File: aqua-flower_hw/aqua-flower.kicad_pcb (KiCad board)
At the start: 2 copper layers, 44 parts, among them Q1 NPN, Q2 IRLML6302, Q3 IRLML6302, Q4 IRLML6302, Q5 IRLML6302, SW1 BUTTON, SW2 BUTTON, SW3 BUTTON, SW4 BUTTON, SW5 BUTTON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

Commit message: Now everything is ok. + Add library by the library Wizard. + Found needed in KiCad github.
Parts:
- C1, C10, C11, C2, C3, C4, C5, C6, C7, C8, C9: footprint Capacitors_SMD:C_0603_HandSoldering -> Capacitors:CAP_0603
- DD1: footprint Housings_QFP:LQFP-48_7x7mm_Pitch0.5mm -> LQFP_TQFP:LQFP48
- R1, R2, R3, R4, R5: footprint Resistors_SMD:R_0603_HandSoldering -> Resistors:RES_0603
- moved HOLE1 68.3 mm to (215.9, 110.5)
- moved C6 61.4 mm to (156.0, 104.5)
- moved C7 61.0 mm to (152.4, 104.5)
- moved DD1 58.6 mm to (188.9, 63.5)
- moved SW6 56.4 mm to (207.3, 62.5)
- moved SW2 55.4 mm to (182.5, 98.5)
- moved C9 54.0 mm to (148.9, 104.5)
- moved C4 53.2 mm to (159.5, 106.0)
- moved HOLE2 51.9 mm to (120.7, 58.4)
- moved HOLE3 49.2 mm to (120.7, 108.0)
- moved C2 48.5 mm to (166.6, 106.0)
- moved R2 43.6 mm to (189.0, 95.5)
- moved C1 40.6 mm to (170.2, 104.7)
- moved XL5 38.6 mm to (136.0, 101.3)
- moved C3 38.3 mm to (163.1, 106.0)
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
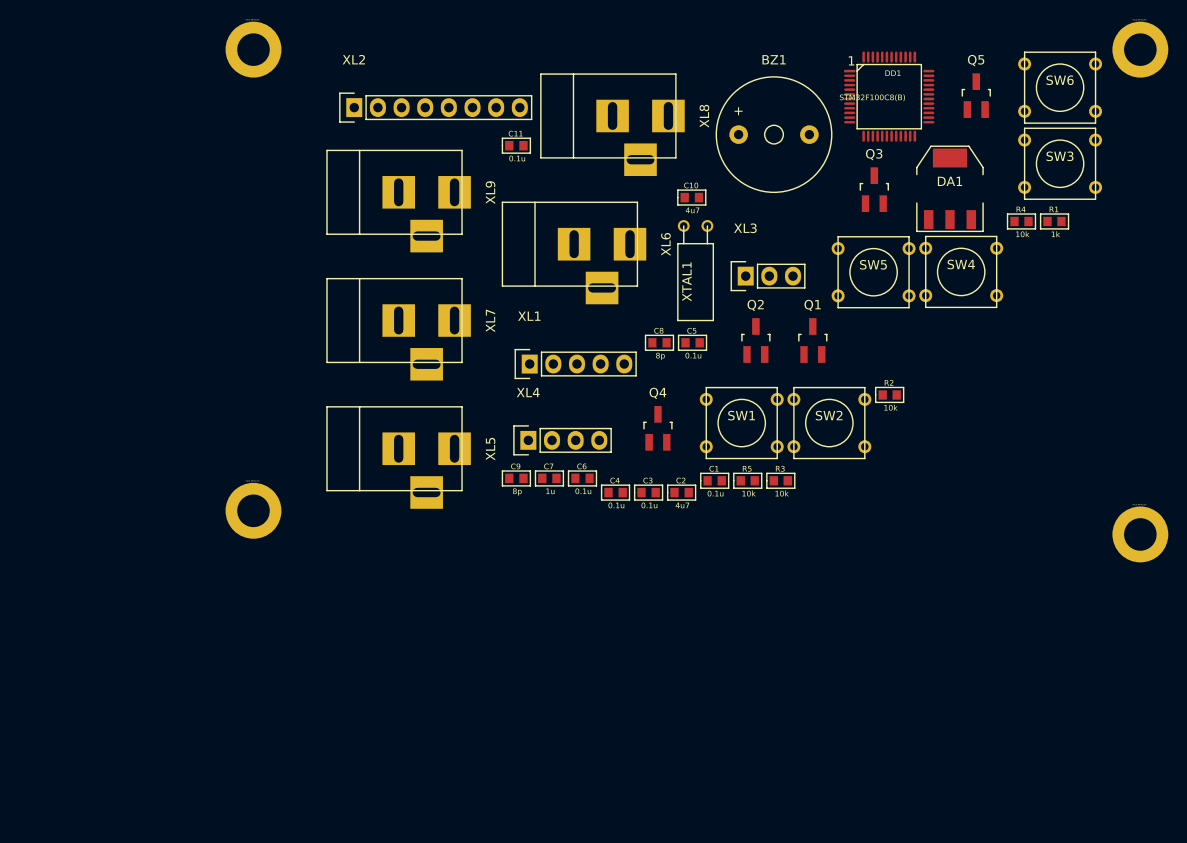
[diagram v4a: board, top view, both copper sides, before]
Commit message: Export to TopoR from KiCAD
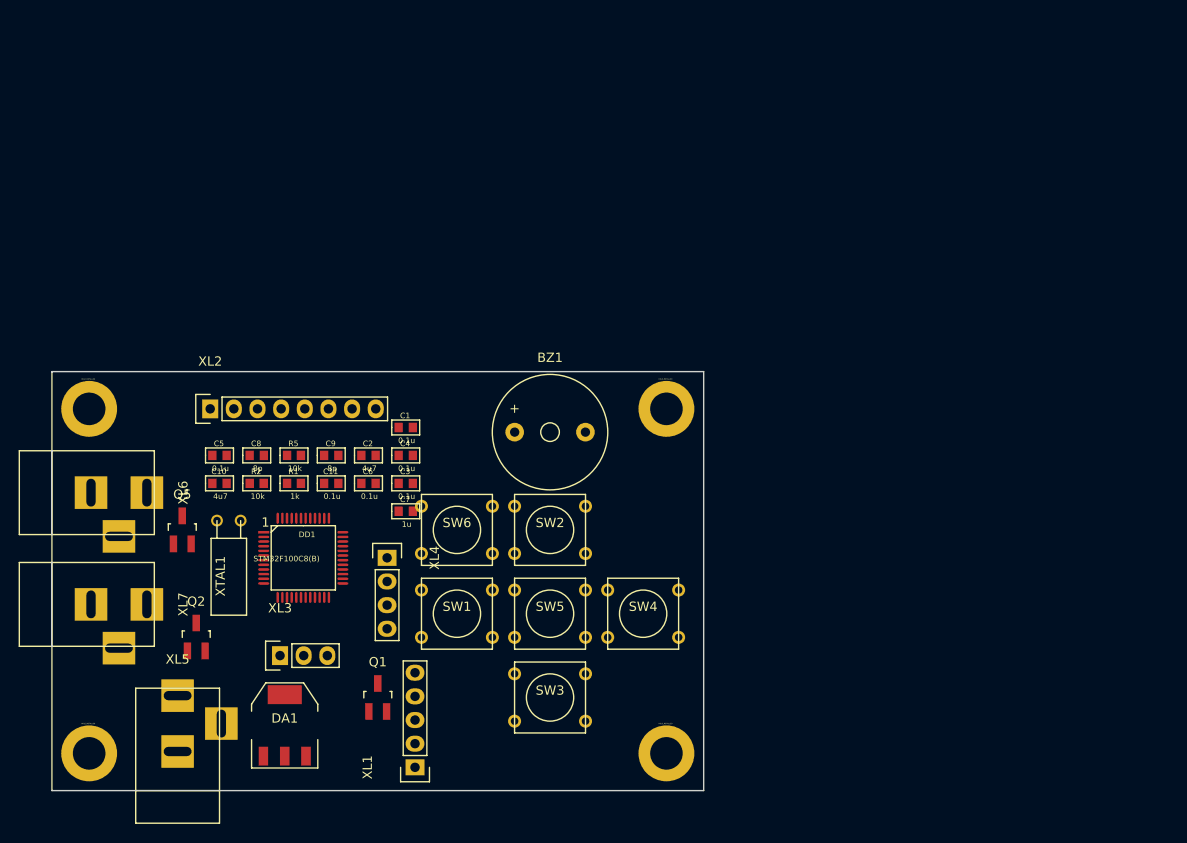
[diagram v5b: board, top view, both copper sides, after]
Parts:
- removed Q3, Q4: IRLML6302, TO_SOT_Packages_SMD:SOT-23_Handsoldering
- removed R3, R4: 10k, Resistors:RES_0603
- removed XL8, XL9: CONN_3, Connect:BARREL_JACK
- moved HOLE4 119.3 mm to (103.0, 97.0)
- moved Q5 97.2 mm to (113.0, 110.0)
- moved DA1 91.8 mm to (124.0, 131.0)
- moved R1 86.4 mm to (125.0, 105.0)
- moved SW6 80.3 mm to (142.5, 110.0)
- moved DD1 80.1 mm to (126.0, 113.0)
- moved SW3 79.3 mm to (152.5, 128.0)
- moved R2 68.6 mm to (121.0, 105.0)
- moved Q2 68.0 mm to (114.5, 121.5)
- moved XL3 64.5 mm to (123.5, 123.5)
- moved Q1 60.4 mm to (134.0, 128.0)
- moved C10 59.3 mm to (117.0, 105.0)
- moved XTAL1 59.3 mm to (118.0, 109.0)
- moved HOLE2 58.8 mm to (165.0, 97.0)
- moved XL6 58.3 mm to (103.0, 106.0)
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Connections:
- DD1 pad 12: /CH3_POWER -> Net-(DD1-Pad12)
- DD1 pad 13: /CH4_POWER -> Net-(DD1-Pad13)
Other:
- board outline added: 70 x 45 mm

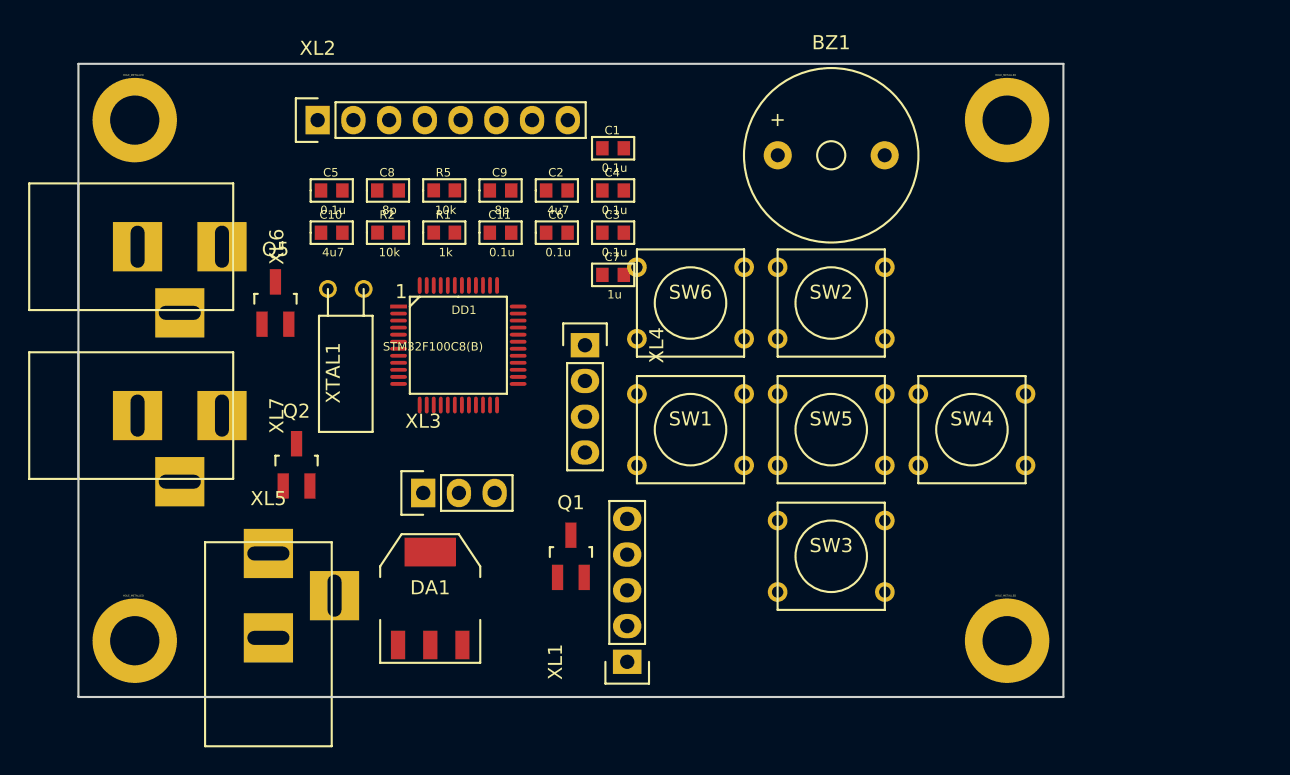
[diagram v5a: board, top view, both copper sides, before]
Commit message: Add eeprom
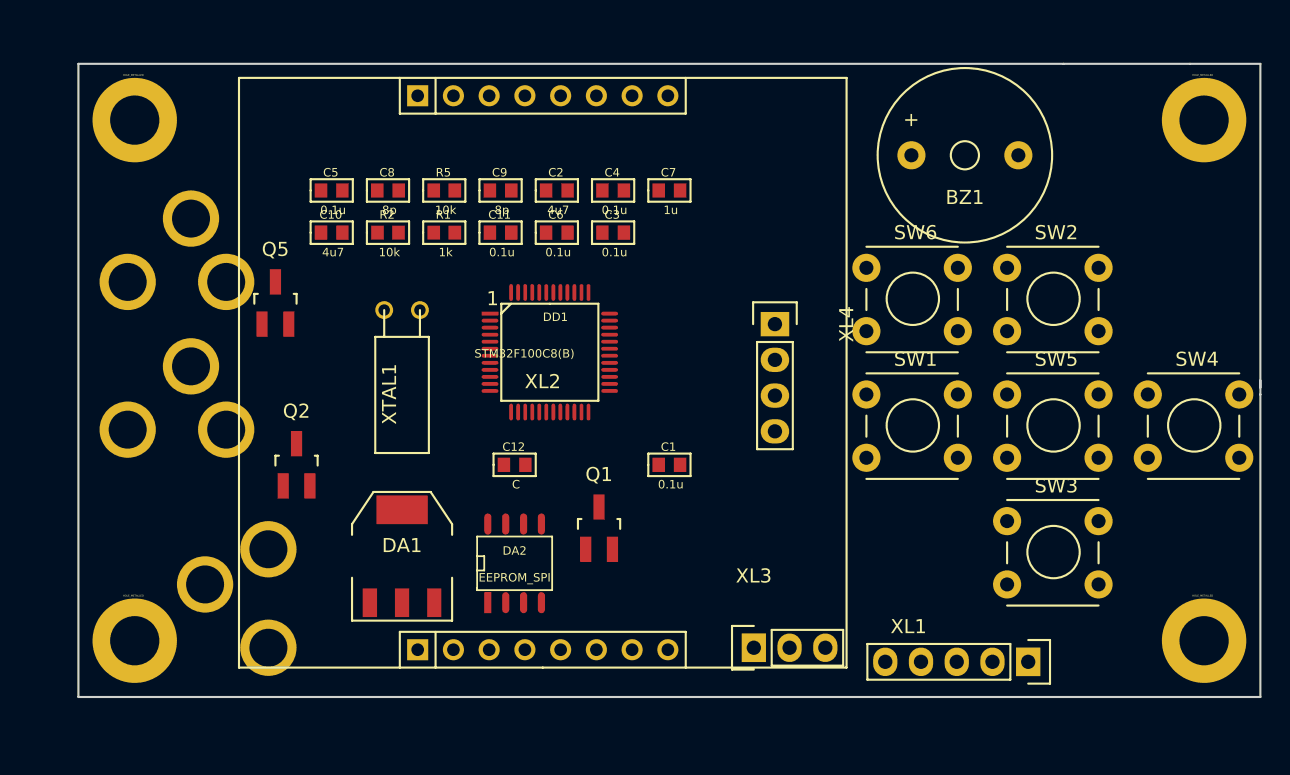
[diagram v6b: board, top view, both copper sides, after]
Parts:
- added C12: C, Capacitors:CAP_0603, F.Cu at (130.0, 121.5)
- added DA2: EEPROM_SPI, SO_DIL_TSSOP:SO8, F.Cu at (130.0, 128.5)
- SW1, SW2, SW3, SW4, SW5, SW6: footprint Buttons_Switches_ThroughHole:SW_PUSH_SMALL -> BtnsSwitches:PUSH_THRHOLE_3-1825910-5
- XL2: footprint Socket_Strips:Socket_Strip_Straight_1x08 -> Display:84x48_LCD_Module
- XL5, XL6, XL7: value CONN_3 -> BARREL_SOCKET; footprint Connect:BARREL_JACK -> Connectors:Barrel; moved to B.Cu
- moved XL1 28.5 mm to (166.5, 135.5), turned to 180 degrees
- moved XL3 25.9 mm to (147.0, 134.5)
- moved XL5 25.7 mm to (109.5, 108.5), turned to 0 degrees
- moved C1 22.9 mm to (141.0, 121.5)
- moved XL2 16.3 mm to (132.0, 94.0)
- moved XL6 14.5 mm to (109.5, 119.0)
- moved HOLE1 14.0 mm to (179.0, 134.0)
- moved HOLE2 14.0 mm to (179.0, 97.0)
- moved XL4 13.6 mm to (148.5, 111.5)
- moved XL7 13.4 mm to (112.5, 127.5), turned to 90 degrees
- moved SW1 12.3 mm to (154.5, 121.5)
- moved SW2 12.3 mm to (164.5, 112.5)
- moved SW3 12.3 mm to (164.5, 130.5)
- moved SW4 12.3 mm to (174.5, 121.5)
- moved SW5 12.3 mm to (164.5, 121.5)
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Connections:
- DD1 pad 12: Net-(DD1-Pad12) -> /EE_HOLD
- DD1 pad 13: Net-(DD1-Pad13) -> /EE_WP
- DD1 pad 42: Net-(DD1-Pad42) -> /EE_CS
- DD1 pad 43: Net-(DD1-Pad43) -> /EE_MISO
- DD1 pad 45: Net-(DD1-Pad45) -> /EE_MOSI
- DD1 pad 46: Net-(DD1-Pad46) -> /EE_SCK
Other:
- board size 70 x 45 mm -> 84 x 45 mm

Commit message: Replace straight pin connectors
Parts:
- XL1: footprint Socket_Strips:Socket_Strip_Straight_1x05 -> Connectors:PLS-5
- XL3: footprint Socket_Strips:Socket_Strip_Straight_1x03 -> Connectors:PLS-3
- XL4: footprint Socket_Strips:Socket_Strip_Straight_1x04 -> Connectors:PLS-4
- moved XL7 20.7 mm to (109.5, 107.0), turned to 0 degrees
- moved XL5 19.3 mm to (113.0, 127.5), turned to 90 degrees
- moved C3 16.3 mm to (135.5, 121.2), turned to 180 degrees
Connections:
- Q2 pad 3: Net-(Q2-Pad3) -> /12V
- Q5 pad 3: Net-(Q5-Pad3) -> /12V
- XL6 pad PWR: Net-(Q5-Pad3) -> /12V
- XL7 pad PWR: Net-(Q2-Pad3) -> /12V
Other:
- outline, holes or cut-outs redrawn
- net class 12V added: clearance 0.3, trace_width 0.7, via_dia 0.8, via_drill 0.4
- net class Default: via_dia 0.6 -> 0.8
- net class PWR added: clearance 0.3, trace_width 0.5, via_dia 0.8, via_drill 0.4
- rule via_min_size: 0.4 -> 0.7

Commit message: PCB finalize. Ready to production.
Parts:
- C10: value 4u7 -> 10u; footprint Capacitors:CAP_0603 -> Capacitors:CAP_0805
- C12: value C -> 0.1u
- XL1: value CONN_5 -> CONN_6; footprint Connectors:PLS-5 -> Connectors:PLS-6
- moved XL1 49.5 mm to (121.4, 115.0), turned to 90 degrees
- moved XL3 35.1 mm to (155.3, 100.4), turned to 90 degrees
- moved Q1 27.3 mm to (152.1, 104.0), turned to 270 degrees
- moved C5 25.9 mm to (142.2, 108.1), turned to 270 degrees
- moved DA2 22.7 mm to (147.9, 114.6)
- moved C12 20.4 mm to (145.4, 108.1), turned to 270 degrees
- moved C10 19.5 mm to (116.8, 124.5), turned to 270 degrees
- moved C4 19.3 mm to (137.0, 121.3)
- moved C2 19.2 mm to (126.7, 120.1), turned to 270 degrees
- moved R5 16.9 mm to (116.0, 116.3), turned to 180 degrees
- moved XL4 16.9 mm to (155.2, 127.0)
- moved R1 15.9 mm to (140.6, 108.1), turned to 270 degrees
- moved C11 15.6 mm to (125.1, 120.1), turned to 270 degrees
- moved XTAL1 14.6 mm to (134.6, 103.2), turned to 90 degrees
- moved Q2 14.5 mm to (115.2, 107.0), turned to 90 degrees
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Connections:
- Q2 pad 3: /12V -> /PUMP2
- Q5 pad 3: /12V -> /PUMP1
- XL1 pad 2: /CC_SCK -> /CC_MOSI
- XL1 pad 3: /CC_CS -> /CC_MISO
- XL1 pad 4: /CC_MISO -> /CC_SCK
- XL1 pad 5: /CC_MOSI -> /CC_CS
- XL6 pad PWR: /12V -> /PUMP1
- XL7 pad PWR: /12V -> /PUMP2
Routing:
- net GND: track 0.00 -> 494.0 mm, vias 0 -> 6
- net +3.3V: track 0.00 -> 179.8 mm, vias 0 -> 7
- net /BTN_UP: track 0.00 -> 58.5 mm, vias 0 -> 2
- net /BTN_OK: track 0.00 -> 57.8 mm, vias 0 -> 1
- net /BTN_RIGHT: track 0.00 -> 53.8 mm
- net /BTN_CANCEL: track 0.00 -> 49.1 mm, vias 0 -> 2
- net /BTN_DOWN: track 0.00 -> 45.0 mm
- net +12V: track 0.00 -> 43.1 mm, vias 0 -> 3
- net /DBG_TX: track 0.00 -> 39.8 mm, vias 0 -> 1
- net /DBG_RX: track 0.00 -> 37.2 mm, vias 0 -> 1
- net /BTN_LEFT: track 0.00 -> 33.8 mm
- net /SWDIO: track 0.00 -> 29.9 mm, vias 0 -> 1
- net /CH1_POWER: track 0.00 -> 29.4 mm, vias 0 -> 2
- net /EE_WP: track 0.00 -> 27.4 mm, vias 0 -> 2
- net /LCD_CLK: track 0.00 -> 26.6 mm, vias 0 -> 2
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- added copper zone on B.Cu, net GND
- added copper zone on F.Cu, net GND
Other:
- board text added: "Aqua Flower v.1"
